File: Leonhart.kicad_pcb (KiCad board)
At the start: 8 copper layers, 34 parts, among them J1001 TC2050, J1002 Conn_01x03_Pin, J2001 TC2050, J2002 Conn_01x06_Pin, J2003 SMA-KWE901, J3002 TC2050, J3003 Conn_01x06_Pin, J3004 SMA-KWE901, J7001 USB_C_Receptacle_USB2.0_16P, J7002 USB_A, J7003 Micro_SD_Card_Det1, Q6001 DMG1012T, Q6002 DMG1012T, U1001 AM6231ASGGGAALW, U1002 SN74LVC2G241DCUR, U1003 AT24C32D-STUM-T, U2001 CC2652PSIP, U3001 nRF52840, U4001 TPS6521903RHBR, U4002 TLV62595DMQR, U5001 K4AAG165WA-BCWE, U6001 HR911130A, U6002 RTL8211F-CG, U7001 TVS0500DRVR, U7002 EMMC16G-TB29-PZ90, U7004 TPD3S014, U7005 TPS22918DBVR, X1001 32.768kHz, X1002 25MHz, X3001 32.768kHz, X3002 32MHz, X6001 ECS-2520MV-250-BN-TR

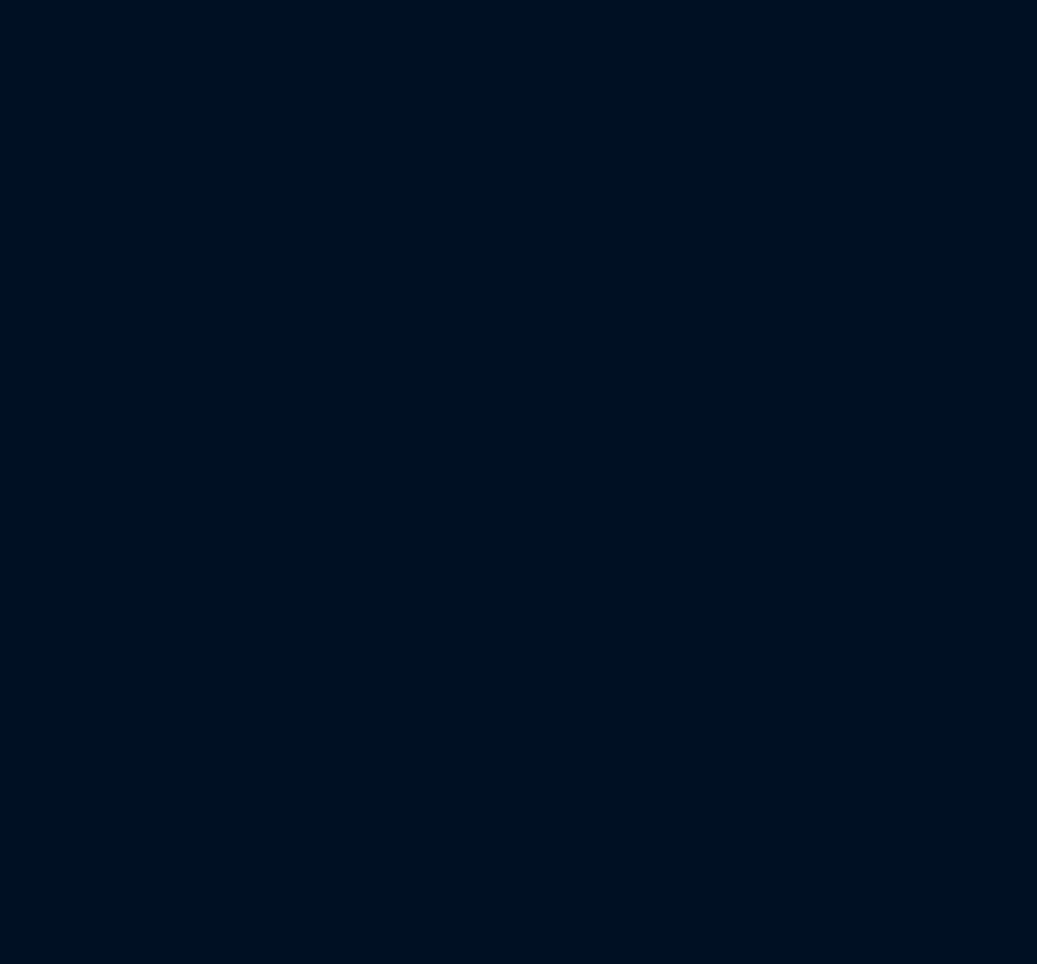
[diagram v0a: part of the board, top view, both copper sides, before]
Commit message: Added capcitor footprints
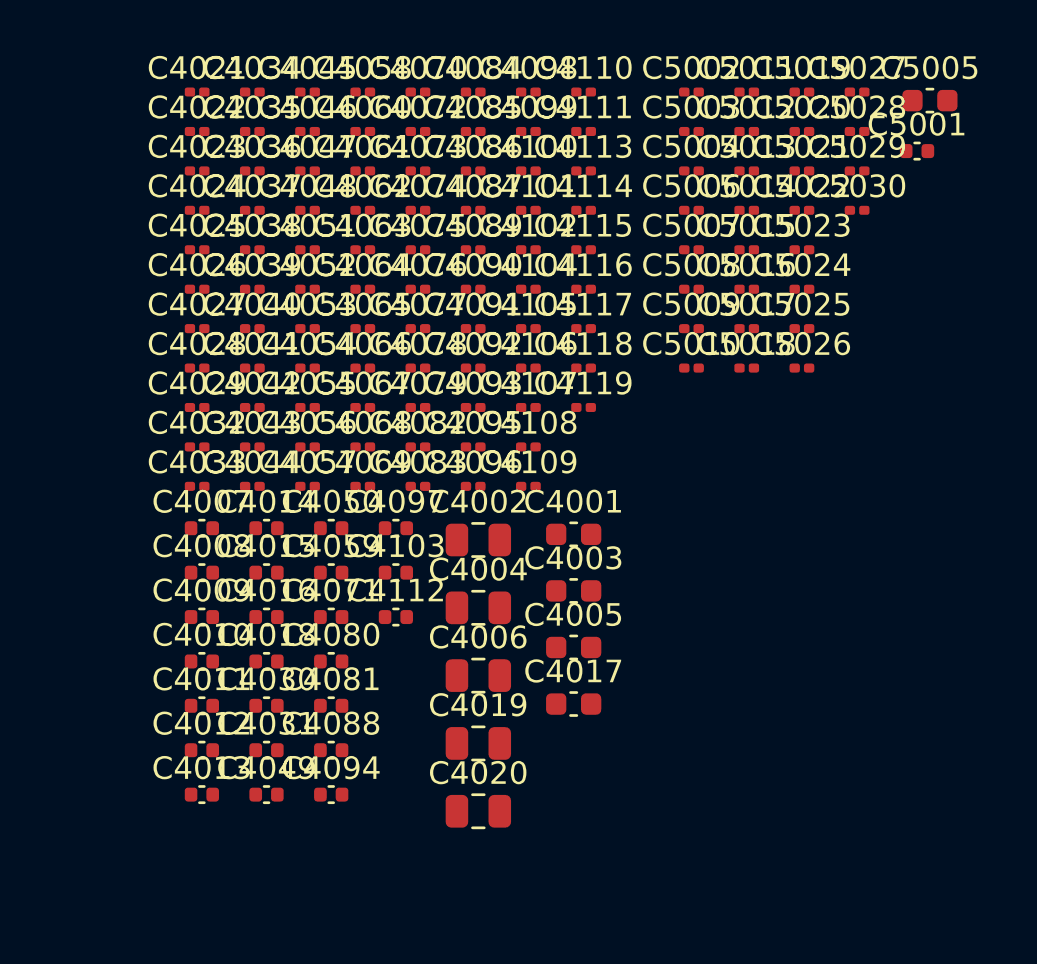
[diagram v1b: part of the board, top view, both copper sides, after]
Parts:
- added C4001: 10u, Capacitor_SMD:C_0603_1608Metric, F.Cu at (232.0, 70.1)
- added C4002: 47u, Capacitor_SMD:C_0805_2012Metric, F.Cu at (227.8, 70.4)
- added C4003: 10u, Capacitor_SMD:C_0603_1608Metric, F.Cu at (232.0, 72.6)
- added C4004: 47u, Capacitor_SMD:C_0805_2012Metric, F.Cu at (227.8, 73.4)
- added C4005: 10u, Capacitor_SMD:C_0603_1608Metric, F.Cu at (232.0, 75.1)
- added C4006: 47u, Capacitor_SMD:C_0805_2012Metric, F.Cu at (227.8, 76.4)
- added C4007: 2.2u, Capacitor_SMD:C_0402_1005Metric, F.Cu at (215.5, 69.8)
- added C4008: 2.2u, Capacitor_SMD:C_0402_1005Metric, F.Cu at (215.5, 71.8)
- added C4009: 2.2u, Capacitor_SMD:C_0402_1005Metric, F.Cu at (215.5, 73.8)
- added C4010: 2.2u, Capacitor_SMD:C_0402_1005Metric, F.Cu at (215.5, 75.8)
- added C4011: 2.2u, Capacitor_SMD:C_0402_1005Metric, F.Cu at (215.5, 77.7)
- added C4012: 2.2u, Capacitor_SMD:C_0402_1005Metric, F.Cu at (215.5, 79.7)
- added C4013: 2.2u, Capacitor_SMD:C_0402_1005Metric, F.Cu at (215.5, 81.7)
- added C4014: 2.2u, Capacitor_SMD:C_0402_1005Metric, F.Cu at (218.4, 69.8)
- added C4015: 2.2u, Capacitor_SMD:C_0402_1005Metric, F.Cu at (218.4, 71.8)
- added C4016: 2.2u, Capacitor_SMD:C_0402_1005Metric, F.Cu at (218.4, 73.8)
- added C4017: 10u, Capacitor_SMD:C_0603_1608Metric, F.Cu at (232.0, 77.7)
- added C4018: 120p, Capacitor_SMD:C_0402_1005Metric, F.Cu at (218.4, 75.8)
- added C4019: 22u, Capacitor_SMD:C_0805_2012Metric, F.Cu at (227.8, 79.4)
- added C4020: 22u, Capacitor_SMD:C_0805_2012Metric, F.Cu at (227.8, 82.4)
- added C4021: 1u, Capacitor_SMD:C_0201_0603Metric, F.Cu at (215.3, 50.5)
- added C4022: 1u, Capacitor_SMD:C_0201_0603Metric, F.Cu at (215.3, 52.2)
- added C4023: 1u, Capacitor_SMD:C_0201_0603Metric, F.Cu at (215.3, 54.0)
- added C4024: 1u, Capacitor_SMD:C_0201_0603Metric, F.Cu at (215.3, 55.7)
- added C4025: 1u, Capacitor_SMD:C_0201_0603Metric, F.Cu at (215.3, 57.5)
- added C4026: 1u, Capacitor_SMD:C_0201_0603Metric, F.Cu at (215.3, 59.2)
- added C4027: 1u, Capacitor_SMD:C_0201_0603Metric, F.Cu at (215.3, 61.0)
- added C4028: 1u, Capacitor_SMD:C_0201_0603Metric, F.Cu at (215.3, 62.7)
- added C4029: 1u, Capacitor_SMD:C_0201_0603Metric, F.Cu at (215.3, 64.5)
- added C4030: 10u, Capacitor_SMD:C_0402_1005Metric, F.Cu at (218.4, 77.7)
- added C4031: 4.7u, Capacitor_SMD:C_0402_1005Metric, F.Cu at (218.4, 79.7)
- added C4032: 1u, Capacitor_SMD:C_0201_0603Metric, F.Cu at (215.3, 66.2)
- added C4033: 0.1u, Capacitor_SMD:C_0201_0603Metric, F.Cu at (215.3, 68.0)
- added C4034: 0.1u, Capacitor_SMD:C_0201_0603Metric, F.Cu at (217.8, 50.5)
- added C4035: 0.1u, Capacitor_SMD:C_0201_0603Metric, F.Cu at (217.8, 52.2)
- added C4036: 0.1u, Capacitor_SMD:C_0201_0603Metric, F.Cu at (217.8, 54.0)
- added C4037: 0.1u, Capacitor_SMD:C_0201_0603Metric, F.Cu at (217.8, 55.7)
- added C4038: 0.1u, Capacitor_SMD:C_0201_0603Metric, F.Cu at (217.8, 57.5)
- added C4039: 0.1u, Capacitor_SMD:C_0201_0603Metric, F.Cu at (217.8, 59.2)
- added C4040: 0.1u, Capacitor_SMD:C_0201_0603Metric, F.Cu at (217.8, 61.0)
- added C4041: 0.1u, Capacitor_SMD:C_0201_0603Metric, F.Cu at (217.8, 62.7)
- added C4042: 0.1u, Capacitor_SMD:C_0201_0603Metric, F.Cu at (217.8, 64.5)
- added C4043: 0.1u, Capacitor_SMD:C_0201_0603Metric, F.Cu at (217.8, 66.2)
- added C4044: 0.1u, Capacitor_SMD:C_0201_0603Metric, F.Cu at (217.8, 68.0)
- added C4045: 0.1u, Capacitor_SMD:C_0201_0603Metric, F.Cu at (220.2, 50.5)
- added C4046: 0.1u, Capacitor_SMD:C_0201_0603Metric, F.Cu at (220.2, 52.2)
- added C4047: 0.1u, Capacitor_SMD:C_0201_0603Metric, F.Cu at (220.2, 54.0)
- added C4048: 0.1u, Capacitor_SMD:C_0201_0603Metric, F.Cu at (220.2, 55.7)
- added C4049: 10u, Capacitor_SMD:C_0402_1005Metric, F.Cu at (218.4, 81.7)
- added C4050: 4.7u, Capacitor_SMD:C_0402_1005Metric, F.Cu at (221.3, 69.8)
- added C4051: 0.1u, Capacitor_SMD:C_0201_0603Metric, F.Cu at (220.2, 57.5)
- added C4052: 0.1u, Capacitor_SMD:C_0201_0603Metric, F.Cu at (220.2, 59.2)
- added C4053: 0.1u, Capacitor_SMD:C_0201_0603Metric, F.Cu at (220.2, 61.0)
- added C4054: 0.1u, Capacitor_SMD:C_0201_0603Metric, F.Cu at (220.2, 62.7)
- added C4055: 0.1u, Capacitor_SMD:C_0201_0603Metric, F.Cu at (220.2, 64.5)
- added C4056: 0.1u, Capacitor_SMD:C_0201_0603Metric, F.Cu at (220.2, 66.2)
- added C4057: 0.1u, Capacitor_SMD:C_0201_0603Metric, F.Cu at (220.2, 68.0)
- added C4058: 0.1u, Capacitor_SMD:C_0201_0603Metric, F.Cu at (222.7, 50.5)
- added C4059: 4.7u, Capacitor_SMD:C_0402_1005Metric, F.Cu at (221.3, 71.8)
- added C4060: 1u, Capacitor_SMD:C_0201_0603Metric, F.Cu at (222.7, 52.2)
- added C4061: 0.1u, Capacitor_SMD:C_0201_0603Metric, F.Cu at (222.7, 54.0)
- added C4062: 0.1u, Capacitor_SMD:C_0201_0603Metric, F.Cu at (222.7, 55.7)
- added C4063: 0.1u, Capacitor_SMD:C_0201_0603Metric, F.Cu at (222.7, 57.5)
- added C4064: 0.1u, Capacitor_SMD:C_0201_0603Metric, F.Cu at (222.7, 59.2)
- added C4065: 0.1u, Capacitor_SMD:C_0201_0603Metric, F.Cu at (222.7, 61.0)
- added C4066: 0.1u, Capacitor_SMD:C_0201_0603Metric, F.Cu at (222.7, 62.7)
- added C4067: 0.1u, Capacitor_SMD:C_0201_0603Metric, F.Cu at (222.7, 64.5)
- added C4068: 0.1u, Capacitor_SMD:C_0201_0603Metric, F.Cu at (222.7, 66.2)
- added C4069: 0.1u, Capacitor_SMD:C_0201_0603Metric, F.Cu at (222.7, 68.0)
- added C4070: 0.1u, Capacitor_SMD:C_0201_0603Metric, F.Cu at (225.1, 50.5)
- added C4071: 4.7u, Capacitor_SMD:C_0402_1005Metric, F.Cu at (221.3, 73.8)
- added C4072: 1u, Capacitor_SMD:C_0201_0603Metric, F.Cu at (225.1, 52.2)
- added C4073: 0.1u, Capacitor_SMD:C_0201_0603Metric, F.Cu at (225.1, 54.0)
- added C4074: 0.1u, Capacitor_SMD:C_0201_0603Metric, F.Cu at (225.1, 55.7)
- added C4075: 0.1u, Capacitor_SMD:C_0201_0603Metric, F.Cu at (225.1, 57.5)
- added C4076: 0.1u, Capacitor_SMD:C_0201_0603Metric, F.Cu at (225.1, 59.2)
- added C4077: 0.1u, Capacitor_SMD:C_0201_0603Metric, F.Cu at (225.1, 61.0)
- added C4078: 0.1u, Capacitor_SMD:C_0201_0603Metric, F.Cu at (225.1, 62.7)
- added C4079: 0.1u, Capacitor_SMD:C_0201_0603Metric, F.Cu at (225.1, 64.5)
- added C4080: 10u, Capacitor_SMD:C_0402_1005Metric, F.Cu at (221.3, 75.8)
- added C4081: 4.7u, Capacitor_SMD:C_0402_1005Metric, F.Cu at (221.3, 77.7)
- added C4082: 1u, Capacitor_SMD:C_0201_0603Metric, F.Cu at (225.1, 66.2)
- added C4083: 0.1u, Capacitor_SMD:C_0201_0603Metric, F.Cu at (225.1, 68.0)
- added C4084: 0.1u, Capacitor_SMD:C_0201_0603Metric, F.Cu at (227.6, 50.5)
- added C4085: 0.1u, Capacitor_SMD:C_0201_0603Metric, F.Cu at (227.6, 52.2)
- added C4086: 0.1u, Capacitor_SMD:C_0201_0603Metric, F.Cu at (227.6, 54.0)
- added C4087: 0.1u, Capacitor_SMD:C_0201_0603Metric, F.Cu at (227.6, 55.7)
- added C4088: 4.7u, Capacitor_SMD:C_0402_1005Metric, F.Cu at (221.3, 79.7)
- added C4089: 0.1u, Capacitor_SMD:C_0201_0603Metric, F.Cu at (227.6, 57.5)
- added C4090: 0.01u, Capacitor_SMD:C_0201_0603Metric, F.Cu at (227.6, 59.2)
- added C4091: 1u, Capacitor_SMD:C_0201_0603Metric, F.Cu at (227.6, 61.0)
- added C4092: 0.1u, Capacitor_SMD:C_0201_0603Metric, F.Cu at (227.6, 62.7)
- added C4093: 0.01u, Capacitor_SMD:C_0201_0603Metric, F.Cu at (227.6, 64.5)
- added C4094: 4.7u, Capacitor_SMD:C_0402_1005Metric, F.Cu at (221.3, 81.7)
- added C4095: 0.1u, Capacitor_SMD:C_0201_0603Metric, F.Cu at (227.6, 66.2)
- added C4096: 0.01u, Capacitor_SMD:C_0201_0603Metric, F.Cu at (227.6, 68.0)
- added C4097: 4.7u, Capacitor_SMD:C_0402_1005Metric, F.Cu at (224.1, 69.8)
- added C4098: 0.1u, Capacitor_SMD:C_0201_0603Metric, F.Cu at (230.0, 50.5)
- added C4099: 0.01u, Capacitor_SMD:C_0201_0603Metric, F.Cu at (230.0, 52.2)
- added C4100: 1u, Capacitor_SMD:C_0201_0603Metric, F.Cu at (230.0, 54.0)
- added C4101: 0.1u, Capacitor_SMD:C_0201_0603Metric, F.Cu at (230.0, 55.7)
- added C4102: 0.01u, Capacitor_SMD:C_0201_0603Metric, F.Cu at (230.0, 57.5)
- added C4103: 4.7u, Capacitor_SMD:C_0402_1005Metric, F.Cu at (224.1, 71.8)
- added C4104: 0.1u, Capacitor_SMD:C_0201_0603Metric, F.Cu at (230.0, 59.2)
- added C4105: 0.01u, Capacitor_SMD:C_0201_0603Metric, F.Cu at (230.0, 61.0)
- added C4106: 1u, Capacitor_SMD:C_0201_0603Metric, F.Cu at (230.0, 62.7)
- added C4107: 0.1u, Capacitor_SMD:C_0201_0603Metric, F.Cu at (230.0, 64.5)
- added C4108: 0.01u, Capacitor_SMD:C_0201_0603Metric, F.Cu at (230.0, 66.2)
- added C4109: 1u, Capacitor_SMD:C_0201_0603Metric, F.Cu at (230.0, 68.0)
- added C4110: 0.1u, Capacitor_SMD:C_0201_0603Metric, F.Cu at (232.5, 50.5)
- added C4111: 0.01u, Capacitor_SMD:C_0201_0603Metric, F.Cu at (232.5, 52.2)
- added C4112: 4.7u, Capacitor_SMD:C_0402_1005Metric, F.Cu at (224.1, 73.8)
- added C4113: 0.1u, Capacitor_SMD:C_0201_0603Metric, F.Cu at (232.5, 54.0)
- added C4114: 0.01u, Capacitor_SMD:C_0201_0603Metric, F.Cu at (232.5, 55.7)
- added C4115: 1u, Capacitor_SMD:C_0201_0603Metric, F.Cu at (232.5, 57.5)
- added C4116: 0.1u, Capacitor_SMD:C_0201_0603Metric, F.Cu at (232.5, 59.2)
- added C4117: 0.01u, Capacitor_SMD:C_0201_0603Metric, F.Cu at (232.5, 61.0)
- added C4118: 0.1u, Capacitor_SMD:C_0201_0603Metric, F.Cu at (232.5, 62.7)
- added C4119: 0.1u, Capacitor_SMD:C_0201_0603Metric, F.Cu at (232.5, 64.5)
- added C5001: 2.2u, Capacitor_SMD:C_0402_1005Metric, F.Cu at (247.3, 53.1)
- added C5002: 0.1u, Capacitor_SMD:C_0201_0603Metric, F.Cu at (237.3, 50.5)
- added C5003: 0.1u, Capacitor_SMD:C_0201_0603Metric, F.Cu at (237.3, 52.2)
- added C5004: 0.01u, Capacitor_SMD:C_0201_0603Metric, F.Cu at (237.3, 54.0)
- added C5005: 22u, Capacitor_SMD:C_0603_1608Metric, F.Cu at (247.8, 50.9)
- added C5006: 0.1u, Capacitor_SMD:C_0201_0603Metric, F.Cu at (237.3, 55.7)
- added C5007: 0.1u, Capacitor_SMD:C_0201_0603Metric, F.Cu at (237.3, 57.5)
- added C5008: 0.1u, Capacitor_SMD:C_0201_0603Metric, F.Cu at (237.3, 59.2)
- added C5009: 0.1u, Capacitor_SMD:C_0201_0603Metric, F.Cu at (237.3, 61.0)
- added C5010: 0.1u, Capacitor_SMD:C_0201_0603Metric, F.Cu at (237.3, 62.7)
- added C5011: 0.1u, Capacitor_SMD:C_0201_0603Metric, F.Cu at (239.7, 50.5)
- added C5012: 0.1u, Capacitor_SMD:C_0201_0603Metric, F.Cu at (239.7, 52.2)
- added C5013: 0.1u, Capacitor_SMD:C_0201_0603Metric, F.Cu at (239.7, 54.0)
- added C5014: 0.1u, Capacitor_SMD:C_0201_0603Metric, F.Cu at (239.7, 55.7)
- added C5015: 0.1u, Capacitor_SMD:C_0201_0603Metric, F.Cu at (239.7, 57.5)
- added C5016: 0.1u, Capacitor_SMD:C_0201_0603Metric, F.Cu at (239.7, 59.2)
- added C5017: 0.1u, Capacitor_SMD:C_0201_0603Metric, F.Cu at (239.7, 61.0)
- added C5018: 0.1u, Capacitor_SMD:C_0201_0603Metric, F.Cu at (239.7, 62.7)
- added C5019: 0.1u, Capacitor_SMD:C_0201_0603Metric, F.Cu at (242.2, 50.5)
- added C5020: 0.1u, Capacitor_SMD:C_0201_0603Metric, F.Cu at (242.2, 52.2)
- added C5021: 0.1u, Capacitor_SMD:C_0201_0603Metric, F.Cu at (242.2, 54.0)
- added C5022: 1n, Capacitor_SMD:C_0201_0603Metric, F.Cu at (242.2, 55.7)
- added C5023: 1n, Capacitor_SMD:C_0201_0603Metric, F.Cu at (242.2, 57.5)
- added C5024: 100p, Capacitor_SMD:C_0201_0603Metric, F.Cu at (242.2, 59.2)
- added C5025: 100p, Capacitor_SMD:C_0201_0603Metric, F.Cu at (242.2, 61.0)
- added C5026: 47p, Capacitor_SMD:C_0201_0603Metric, F.Cu at (242.2, 62.7)
- added C5027: 47p, Capacitor_SMD:C_0201_0603Metric, F.Cu at (244.6, 50.5)
- added C5028: 10p, Capacitor_SMD:C_0201_0603Metric, F.Cu at (244.6, 52.2)
- added C5029: 10p, Capacitor_SMD:C_0201_0603Metric, F.Cu at (244.6, 54.0)
- added C5030: 10p, Capacitor_SMD:C_0201_0603Metric, F.Cu at (244.6, 55.7)

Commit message: Added almost all passive component footprints
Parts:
- added C1001: 0.1u, Capacitor_SMD:C_0201_0603Metric, F.Cu at (269.6, 70.0)
- added C1002: 20p, Capacitor_SMD:C_0402_1005Metric, F.Cu at (266.9, 70.1)
- added C1003: 20p, Capacitor_SMD:C_0402_1005Metric, F.Cu at (266.9, 72.1)
- added C1004: 18p, Capacitor_SMD:C_0402_1005Metric, F.Cu at (266.9, 74.1)
- added C1005: 0.1u, Capacitor_SMD:C_0201_0603Metric, F.Cu at (269.6, 71.8)
- added C1006: 18p, Capacitor_SMD:C_0402_1005Metric, F.Cu at (266.9, 76.0)
- added C1007: 0.1u, Capacitor_SMD:C_0201_0603Metric, F.Cu at (269.6, 73.5)
- added C1008: C, Capacitor_SMD:C_0402_1005Metric, F.Cu at (129.7, 165.6)
- added C1009: C, Capacitor_SMD:C_0402_1005Metric, F.Cu at (129.7, 167.6)
- added C2001: 0.1u, Capacitor_SMD:C_0201_0603Metric, F.Cu at (266.7, 79.9)
- added C2002: 15p, Capacitor_SMD:C_0201_0603Metric, F.Cu at (266.7, 81.7)
- added C3001: 4.7u, Capacitor_SMD:C_0402_1005Metric, F.Cu at (121.4, 169.2)
- added C3002: 0.1u, Capacitor_SMD:C_0201_0603Metric, F.Cu at (125.1, 165.5)
- added C3003: 100p, Capacitor_SMD:C_0201_0603Metric, F.Cu at (125.1, 167.2)
- added C3004: 0.1u, Capacitor_SMD:C_0201_0603Metric, F.Cu at (185.7, 51.0)
- added C3005: 1u, Capacitor_SMD:C_0603_1608Metric, F.Cu at (182.4, 51.3)
- added C3006: 47n, Capacitor_SMD:C_0201_0603Metric, F.Cu at (185.7, 52.7)
- added C3007: 4.7u, Capacitor_SMD:C_0603_1608Metric, F.Cu at (182.4, 53.8)
- added C3008: 0.8p, Capacitor_SMD:C_0201_0603Metric, F.Cu at (185.7, 54.5)
- added C3009: 0.5p, Capacitor_SMD:C_0201_0603Metric, F.Cu at (185.7, 56.2)
- added C3011: 8p, Capacitor_SMD:C_0201_0603Metric, F.Cu at (185.7, 58.0)
- added C3012: 8p, Capacitor_SMD:C_0201_0603Metric, F.Cu at (188.1, 51.0)
- added C3013: 12p, Capacitor_SMD:C_0201_0603Metric, F.Cu at (188.1, 52.7)
- added C3014: 12p, Capacitor_SMD:C_0201_0603Metric, F.Cu at (188.1, 54.5)
- added C3015: 0.1u, Capacitor_SMD:C_0201_0603Metric, F.Cu at (188.1, 56.2)
- added C3016: 1u, Capacitor_SMD:C_0603_1608Metric, F.Cu at (182.4, 56.4)
- added C3017: 0.1u, Capacitor_SMD:C_0201_0603Metric, F.Cu at (188.1, 58.0)
- added C3018: 0.1u, Capacitor_SMD:C_0201_0603Metric, F.Cu at (190.6, 51.0)
- added C3019: 0.1u, Capacitor_SMD:C_0201_0603Metric, F.Cu at (190.6, 52.7)
- added C7001: 4.7u, Capacitor_SMD:C_0402_1005Metric, F.Cu at (258.1, 76.2)
- added C7002: 0.1u, Capacitor_SMD:C_0201_0603Metric, F.Cu at (250.5, 70.0)
- added C7003: 0.1u, Capacitor_SMD:C_0201_0603Metric, F.Cu at (250.5, 71.8)
- added C7004: 0.1u, Capacitor_SMD:C_0201_0603Metric, F.Cu at (250.5, 73.5)
- added C7005: 0.1u, Capacitor_SMD:C_0201_0603Metric, F.Cu at (250.5, 75.3)
- added C7006: 0.1u, Capacitor_SMD:C_0201_0603Metric, F.Cu at (250.5, 77.0)
- added C7007: 0.1u, Capacitor_SMD:C_0201_0603Metric, F.Cu at (252.9, 70.0)
- added C7008: 0.1u, Capacitor_SMD:C_0201_0603Metric, F.Cu at (252.9, 71.8)
- added C7009: 0.1u, Capacitor_SMD:C_0201_0603Metric, F.Cu at (252.9, 73.5)
- added C7010: 0.1u, Capacitor_SMD:C_0201_0603Metric, F.Cu at (252.9, 75.3)
- added C7011: 4.7u, Capacitor_SMD:C_0402_1005Metric, F.Cu at (258.1, 78.1)
- added C7012: 10u, Capacitor_SMD:C_0603_1608Metric, F.Cu at (261.5, 76.4)
- added C7013: 0.1u, Capacitor_SMD:C_0201_0603Metric, F.Cu at (252.9, 77.0)
- added C7014: 0.1u, Capacitor_SMD:C_0201_0603Metric, F.Cu at (255.4, 70.0)
- added C7015: 10u, Capacitor_SMD:C_0603_1608Metric, F.Cu at (261.5, 78.9)
- added C7016: 0.1u, Capacitor_SMD:C_0201_0603Metric, F.Cu at (255.4, 71.8)
- added C7017: 100u, Capacitor_SMD:C_1206_3216Metric, F.Cu at (252.1, 79.6)
- added C7018: 4.7u, Capacitor_SMD:C_0402_1005Metric, F.Cu at (258.1, 80.1)
- added C7019: 0.1u, Capacitor_SMD:C_0201_0603Metric, F.Cu at (255.4, 73.5)
- added C7020: 0.1u, Capacitor_SMD:C_0201_0603Metric, F.Cu at (255.4, 75.3)
- added C7021: 22u, Capacitor_SMD:C_0805_2012Metric, F.Cu at (258.9, 70.7)
- added C7022: 22u, Capacitor_SMD:C_0805_2012Metric, F.Cu at (258.9, 73.7)
- added D1001: D, Diode_SMD:D_SOD-523, F.Cu at (150.2, 45.6)
- added D1002: D_TVS, Diode_SMD:D_SOD-882, F.Cu at (126.7, 46.6)
- added D1003: D_TVS, Diode_SMD:D_SOD-882, F.Cu at (126.7, 49.0)
- added D1004: D, Diode_SMD:D_SOD-523, F.Cu at (150.2, 48.1)
- added D1005: D, Diode_SMD:D_SOD-523, F.Cu at (150.2, 50.5)
- added D1006: D, Diode_SMD:D_SOD-523, F.Cu at (150.2, 53.0)
- added D2001: D, Diode_SMD:D_SOD-523, F.Cu at (155.8, 45.6)
- added D2002: D, Diode_SMD:D_SOD-523, F.Cu at (155.8, 48.1)
- added D2003: D, Diode_SMD:D_SOD-523, F.Cu at (155.8, 50.5)
- added D6001: D, Diode_SMD:D_SOD-523, F.Cu at (155.8, 55.0)
- added D6002: D, Diode_SMD:D_SOD-523, F.Cu at (155.8, 57.5)
- added D6003: D, Diode_SMD:D_SOD-523, F.Cu at (155.8, 59.9)
- added D7001: D_TVS, Diode_SMD:D_SOD-882, F.Cu at (116.6, 46.6)
- added D7002: D_TVS, Diode_SMD:D_SOD-882, F.Cu at (116.6, 49.0)
- added D7003: D, Diode_SMD:D_SOD-523, F.Cu at (144.6, 45.6)
- added D7004: D, Diode_SMD:D_SOD-523, F.Cu at (144.6, 48.1)
- added D7005: D, Diode_SMD:D_SOD-523, F.Cu at (144.6, 50.5)
- added D7006: D_TVS, Diode_SMD:D_SOD-882, F.Cu at (116.6, 51.3)
- added D7007: D_TVS, Diode_SMD:D_SOD-882, F.Cu at (119.3, 46.6)
- added D7008: D_TVS, Diode_SMD:D_SOD-882, F.Cu at (119.3, 49.0)
- added D7009: D_TVS, Diode_SMD:D_SOD-882, F.Cu at (119.3, 51.3)
- added D7010: D_TVS, Diode_SMD:D_SOD-882, F.Cu at (122.0, 46.6)
- added D7011: D_TVS, Diode_SMD:D_SOD-882, F.Cu at (122.0, 49.0)
- added D7012: D_TVS, Diode_SMD:D_SOD-882, F.Cu at (122.0, 51.3)
- added D7013: D, Diode_SMD:D_SOD-523, F.Cu at (144.6, 53.0)
- added D7014: D, Diode_SMD:D_SOD-523, F.Cu at (144.6, 55.5)
- added FB2001: 120R, Resistor_SMD:R_0402_1005Metric, F.Cu at (259.4, 100.4)
- added FB3001: 120R, Resistor_SMD:R_0402_1005Metric, F.Cu at (229.7, 129.8)
- added FB4001: 120R, Resistor_SMD:R_0402_1005Metric, F.Cu at (245.8, 100.4)
- added FB4002: 120R, Resistor_SMD:R_0402_1005Metric, F.Cu at (245.8, 102.4)
- added FB4003: 120R, Resistor_SMD:R_0402_1005Metric, F.Cu at (245.8, 104.4)
- added FB4004: 120R, Resistor_SMD:R_0402_1005Metric, F.Cu at (245.8, 106.4)
- added FB4005: 120R, Resistor_SMD:R_0402_1005Metric, F.Cu at (245.8, 108.3)
- added FB4006: 120R, Resistor_SMD:R_0402_1005Metric, F.Cu at (245.8, 110.3)
- added FB4007: 120R, Resistor_SMD:R_0402_1005Metric, F.Cu at (245.8, 112.3)
- added FB4008: 120R, Resistor_SMD:R_0402_1005Metric, F.Cu at (248.7, 100.4)
- added FB4009: 120R, Resistor_SMD:R_0402_1005Metric, F.Cu at (248.7, 102.4)
- added FB4010: 120R, Resistor_SMD:R_0402_1005Metric, F.Cu at (248.7, 104.4)
- added FB4011: 120R, Resistor_SMD:R_0402_1005Metric, F.Cu at (248.7, 106.4)
- added FB5001: 120R, Resistor_SMD:R_0402_1005Metric, F.Cu at (229.7, 118.3)
- added FB6001: 120R, Resistor_SMD:R_0402_1005Metric, F.Cu at (240.4, 118.3)
- added FB6002: 120R, Resistor_SMD:R_0402_1005Metric, F.Cu at (240.4, 120.3)
- added FB6003: 120R, Resistor_SMD:R_0402_1005Metric, F.Cu at (240.4, 122.3)
- added L3001: 10u, Inductor_SMD:L_0603_1608Metric, F.Cu at (182.4, 58.9)
- added L3002: 15n, Inductor_SMD:L_0402_1005Metric, F.Cu at (185.9, 59.8)
- added L3003: 10u, Inductor_SMD:L_0603_1608Metric, F.Cu at (182.4, 61.4)
- added L3004: 4.7n, Inductor_SMD:L_0201_0603Metric, F.Cu at (190.6, 54.5)
- added L4001: 0.33u, Inductor_SMD:L_1008_2520Metric, F.Cu at (100.1, 46.1)
- added L4002: 0.47u, Inductor_SMD:L_1008_2520Metric, F.Cu at (100.1, 49.9)
- added L4003: 0.47u, Inductor_SMD:L_1008_2520Metric, F.Cu at (100.1, 53.6)
- added L4004: 0.47u, Inductor_SMD:L_1008_2520Metric, F.Cu at (100.1, 57.4)
- added R1001: 10k, Resistor_SMD:R_0402_1005Metric, F.Cu at (245.8, 116.3)
- added R1002: 10k, Resistor_SMD:R_0402_1005Metric, F.Cu at (245.8, 118.3)
- added R1003: 10k, Resistor_SMD:R_0402_1005Metric, F.Cu at (245.8, 120.3)
- added R1004: 10k, Resistor_SMD:R_0402_1005Metric, F.Cu at (245.8, 122.3)
- added R1005: 10k, Resistor_SMD:R_0402_1005Metric, F.Cu at (245.8, 124.3)
- added R1006: 10k, Resistor_SMD:R_0402_1005Metric, F.Cu at (245.8, 126.3)
- added R1007: 10k, Resistor_SMD:R_0402_1005Metric, F.Cu at (245.8, 128.3)
- added R1008: 10k, Resistor_SMD:R_0402_1005Metric, F.Cu at (248.7, 116.3)
- added R1009: 2.2k, Resistor_SMD:R_0402_1005Metric, F.Cu at (248.7, 118.3)
- added R1010: 2.2k, Resistor_SMD:R_0402_1005Metric, F.Cu at (248.7, 120.3)
- added R1011: 33R, Resistor_SMD:R_0201_0603Metric, F.Cu at (254.3, 116.2)
- added R1012: 0R, Resistor_SMD:R_0402_1005Metric, F.Cu at (248.7, 122.3)
- added R1013: 10k, Resistor_SMD:R_0402_1005Metric, F.Cu at (248.7, 124.3)
- added R1014: 10k, Resistor_SMD:R_0402_1005Metric, F.Cu at (248.7, 126.3)
- added R1015: R, Resistor_SMD:R_0402_1005Metric, F.Cu at (248.7, 128.3)
- added R1016: R, Resistor_SMD:R_0201_0603Metric, F.Cu at (254.3, 118.0)
- added R1017: R, Resistor_SMD:R_0201_0603Metric, F.Cu at (254.3, 119.7)
- added R1018: 10k, Resistor_SMD:R_0201_0603Metric, F.Cu at (254.3, 121.5)
- added R1019: R, Resistor_SMD:R_0201_0603Metric, F.Cu at (254.3, 123.2)
- added R1020: 10k, Resistor_SMD:R_0201_0603Metric, F.Cu at (254.3, 125.0)
- added R1021: 10k, Resistor_SMD:R_0201_0603Metric, F.Cu at (254.3, 126.7)
- added R1022: R, Resistor_SMD:R_0201_0603Metric, F.Cu at (256.8, 116.2)
- added R1023: 10k, Resistor_SMD:R_0201_0603Metric, F.Cu at (256.8, 118.0)
- added R1024: R, Resistor_SMD:R_0201_0603Metric, F.Cu at (256.8, 119.7)
- added R1025: 10k, Resistor_SMD:R_0201_0603Metric, F.Cu at (256.8, 121.5)
- added R1026: R, Resistor_SMD:R_0201_0603Metric, F.Cu at (256.8, 123.2)
- added R1027: R, Resistor_SMD:R_0201_0603Metric, F.Cu at (256.8, 125.0)
- added R1028: 10k, Resistor_SMD:R_0201_0603Metric, F.Cu at (256.8, 126.7)
- added R1029: R, Resistor_SMD:R_0201_0603Metric, F.Cu at (259.2, 116.2)
- added R1030: 10k, Resistor_SMD:R_0201_0603Metric, F.Cu at (259.2, 118.0)
- added R1031: 10k, Resistor_SMD:R_0201_0603Metric, F.Cu at (259.2, 119.7)
- added R1032: 10k, Resistor_SMD:R_0201_0603Metric, F.Cu at (259.2, 121.5)
- added R1033: 10k, Resistor_SMD:R_0201_0603Metric, F.Cu at (259.2, 123.2)
- added R1034: R, Resistor_SMD:R_0201_0603Metric, F.Cu at (259.2, 125.0)
- added R1035: 10k, Resistor_SMD:R_0201_0603Metric, F.Cu at (259.2, 126.7)
- added R1036: R, Resistor_SMD:R_0201_0603Metric, F.Cu at (261.7, 116.2)
- added R1037: R, Resistor_SMD:R_0201_0603Metric, F.Cu at (261.7, 118.0)
- added R1038: R, Resistor_SMD:R_0201_0603Metric, F.Cu at (261.7, 119.7)
- added R1039: 10k, Resistor_SMD:R_0201_0603Metric, F.Cu at (261.7, 121.5)
- added R1040: 10k, Resistor_SMD:R_0201_0603Metric, F.Cu at (261.7, 123.2)
- added R1041: R, Resistor_SMD:R_0201_0603Metric, F.Cu at (261.7, 125.0)
- added R1042: 10k, Resistor_SMD:R_0201_0603Metric, F.Cu at (261.7, 126.7)
- added R1043: 10k, Resistor_SMD:R_0201_0603Metric, F.Cu at (264.1, 116.2)
- added R1044: R, Resistor_SMD:R_0201_0603Metric, F.Cu at (264.1, 118.0)
- added R1045: 10k, Resistor_SMD:R_0201_0603Metric, F.Cu at (264.1, 119.7)
- added R1046: R, Resistor_SMD:R_0201_0603Metric, F.Cu at (264.1, 121.5)
- added R1047: R, Resistor_SMD:R_0201_0603Metric, F.Cu at (264.1, 123.2)
- added R1048: 10k, Resistor_SMD:R_0402_1005Metric, F.Cu at (251.6, 116.3)
- added R1049: 1k, Resistor_SMD:R_0402_1005Metric, F.Cu at (251.6, 118.3)
- added R1050: 1k, Resistor_SMD:R_0402_1005Metric, F.Cu at (251.6, 120.3)
- added R1051: 1k, Resistor_SMD:R_0402_1005Metric, F.Cu at (251.6, 122.3)
- added R2001: 0R, Resistor_SMD:R_0402_1005Metric, F.Cu at (259.4, 102.4)
- added R2002: 0R, Resistor_SMD:R_0402_1005Metric, F.Cu at (259.4, 104.4)
- added R2003: 0R, Resistor_SMD:R_0402_1005Metric, F.Cu at (259.4, 106.4)
- added R2004: 0R, Resistor_SMD:R_0402_1005Metric, F.Cu at (259.4, 108.3)
- added R3001: 10k, Resistor_SMD:R_0201_0603Metric, F.Cu at (190.6, 56.2)
- added R4001: 0R, Resistor_SMD:R_0402_1005Metric, F.Cu at (248.7, 108.3)
- added R4002: 100k, Resistor_SMD:R_0402_1005Metric, F.Cu at (248.7, 110.3)
- added R4003: 11k, Resistor_SMD:R_0402_1005Metric, F.Cu at (248.7, 112.3)
- added R4004: 10k, Resistor_SMD:R_0402_1005Metric, F.Cu at (251.6, 100.4)
- added R4005: 10k, Resistor_SMD:R_0402_1005Metric, F.Cu at (251.6, 102.4)
- added R4006: 10k, Resistor_SMD:R_0402_1005Metric, F.Cu at (251.6, 104.4)
- added R4007: 10k, Resistor_SMD:R_0402_1005Metric, F.Cu at (251.6, 106.4)
- added R4008: 10k, Resistor_SMD:R_0402_1005Metric, F.Cu at (251.6, 108.3)
- added R4009: 10k, Resistor_SMD:R_0402_1005Metric, F.Cu at (251.6, 110.3)
- added R4010: 10k, Resistor_SMD:R_0402_1005Metric, F.Cu at (251.6, 112.3)
- added R4011: 270k, Resistor_SMD:R_0402_1005Metric, F.Cu at (254.5, 100.4)
- added R4012: 180k, Resistor_SMD:R_0402_1005Metric, F.Cu at (254.5, 102.4)
- added R4013: 100k, Resistor_SMD:R_0402_1005Metric, F.Cu at (254.5, 104.4)
- added R4014: R, Resistor_SMD:R_0402_1005Metric, F.Cu at (254.5, 106.4)
- added R4015: 10k, Resistor_SMD:R_0402_1005Metric, F.Cu at (254.5, 108.3)
- added R5001: 33R, Resistor_SMD:R_0201_0603Metric, F.Cu at (229.5, 124.2)
- added R5002: 33R, Resistor_SMD:R_0201_0603Metric, F.Cu at (229.5, 125.9)
- added R5003: R, Resistor_SMD:R_0402_1005Metric, F.Cu at (229.7, 120.3)
- added R5004: 2.2k, Resistor_SMD:R_0402_1005Metric, F.Cu at (229.7, 122.3)
- added R5005: 10k, Resistor_SMD:R_0402_1005Metric, F.Cu at (232.6, 118.3)
- added R5006: 240R, Resistor_SMD:R_0402_1005Metric, F.Cu at (232.6, 120.3)
- added R5007: 240R, Resistor_SMD:R_0402_1005Metric, F.Cu at (232.6, 122.3)
- added R5008: 1k, Resistor_SMD:R_0402_1005Metric, F.Cu at (235.5, 118.3)
- added R5009: 1k, Resistor_SMD:R_0402_1005Metric, F.Cu at (235.5, 120.3)
- added R5010: 1k, Resistor_SMD:R_0402_1005Metric, F.Cu at (235.5, 122.3)
- added R7001: 22R, Resistor_SMD:R_0201_0603Metric, F.Cu at (241.1, 100.3)
- added R7002: 10k, Resistor_SMD:R_0402_1005Metric, F.Cu at (229.7, 100.4)
- added R7003: 20k, Resistor_SMD:R_0402_1005Metric, F.Cu at (229.7, 102.4)
- added R7004: 49.9k, Resistor_SMD:R_0402_1005Metric, F.Cu at (229.7, 104.4)
- added R7005: 49.9k, Resistor_SMD:R_0402_1005Metric, F.Cu at (229.7, 106.4)
- added R7006: 49.9k, Resistor_SMD:R_0402_1005Metric, F.Cu at (229.7, 108.3)
- added R7007: 49.9k, Resistor_SMD:R_0402_1005Metric, F.Cu at (229.7, 110.3)
- added R7008: 49.9k, Resistor_SMD:R_0402_1005Metric, F.Cu at (229.7, 112.3)
- added R7009: 49.9k, Resistor_SMD:R_0402_1005Metric, F.Cu at (229.7, 114.3)
- added R7010: 49.9k, Resistor_SMD:R_0402_1005Metric, F.Cu at (232.6, 100.4)
- added R7011: 49.9k, Resistor_SMD:R_0402_1005Metric, F.Cu at (232.6, 102.4)
- added R7012: 49.9k, Resistor_SMD:R_0402_1005Metric, F.Cu at (232.6, 104.4)
- added R7013: 49.9k, Resistor_SMD:R_0402_1005Metric, F.Cu at (232.6, 106.4)
- added R7014: 22R, Resistor_SMD:R_0201_0603Metric, F.Cu at (241.1, 102.0)
- added R7015: 499R, Resistor_SMD:R_0402_1005Metric, F.Cu at (232.6, 108.3)
- added R7016: 5.1k, Resistor_SMD:R_0402_1005Metric, F.Cu at (232.6, 110.3)
- added R7017: 5.1k, Resistor_SMD:R_0402_1005Metric, F.Cu at (232.6, 112.3)
- added R7018: 499R, Resistor_SMD:R_0402_1005Metric, F.Cu at (232.6, 114.3)
- added R7019: 49.9k, Resistor_SMD:R_0402_1005Metric, F.Cu at (235.5, 100.4)
- added R7020: 10k, Resistor_SMD:R_0402_1005Metric, F.Cu at (235.5, 102.4)
- added R7021: 20k, Resistor_SMD:R_0402_1005Metric, F.Cu at (235.5, 104.4)
- added R7022: 10k, Resistor_SMD:R_0402_1005Metric, F.Cu at (235.5, 106.4)
- added R7023: 1k, Resistor_SMD:R_0402_1005Metric, F.Cu at (235.5, 108.3)
- added R7024: 10k, Resistor_SMD:R_0402_1005Metric, F.Cu at (235.5, 110.3)
- added R7025: 10k, Resistor_SMD:R_0402_1005Metric, F.Cu at (235.5, 112.3)
- added R7026: 10k, Resistor_SMD:R_0402_1005Metric, F.Cu at (235.5, 114.3)
- added R7027: 10k, Resistor_SMD:R_0402_1005Metric, F.Cu at (238.4, 100.4)
- added R7028: 10k, Resistor_SMD:R_0402_1005Metric, F.Cu at (238.4, 102.4)
- added R7029: 10k, Resistor_SMD:R_0402_1005Metric, F.Cu at (238.4, 104.4)
- added R7030: 10k, Resistor_SMD:R_0402_1005Metric, F.Cu at (238.4, 106.4)
- added R7031: 10k, Resistor_SMD:R_0402_1005Metric, F.Cu at (238.4, 108.3)
- added R8001: 2.2k, Resistor_SMD:R_0402_1005Metric, F.Cu at (240.4, 126.3)
- added R8002: 2.2k, Resistor_SMD:R_0402_1005Metric, F.Cu at (240.4, 128.3)
- added TP1001: TestPoint, TestPoint:TestPoint_Pad_1.0x1.0mm, F.Cu at (243.2, 148.7)
- added TP1002: TestPoint, TestPoint:TestPoint_Pad_1.0x1.0mm, F.Cu at (243.2, 151.7)
- added TP4001: TestPoint, TestPoint:TestPoint_Pad_1.0x1.0mm, F.Cu at (243.2, 140.6)
- added TP4002: TestPoint, TestPoint:TestPoint_Pad_1.0x1.0mm, F.Cu at (243.2, 143.6)
- added TP4003: TestPoint, TestPoint:TestPoint_Pad_1.0x1.0mm, F.Cu at (246.3, 140.6)
- added TP4004: TestPoint, TestPoint:TestPoint_Pad_1.0x1.0mm, F.Cu at (246.3, 143.6)
- added TP4005: TestPoint, TestPoint:TestPoint_Pad_1.0x1.0mm, F.Cu at (249.3, 140.6)
- added TP4006: TestPoint, TestPoint:TestPoint_Pad_1.0x1.0mm, F.Cu at (249.3, 143.6)
- added TP4007: TestPoint, TestPoint:TestPoint_Pad_1.0x1.0mm, F.Cu at (252.4, 140.6)
- added TP4008: TestPoint, TestPoint:TestPoint_Pad_1.0x1.0mm, F.Cu at (252.4, 143.6)
- added TP6001: TestPoint, TestPoint:TestPoint_Pad_1.0x1.0mm, F.Cu at (248.3, 148.7)
- X3002: value 32MHz -> 25MHz
- moved U1001 13.0 mm to (139.0, 73.8)
- moved X3002 9.29 mm to (122.0, 160.2)
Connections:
- X3002 pad 1: /Thread [3]/nRF_XC2 -> /Thread [3]/nRF_XC1
- X3002 pad 2: /Thread [3]/nRF_XC1 -> GND
- X3002 pad 3: (no net) -> /Thread [3]/nRF_XC2
- X3002 pad 4: (no net) -> GND

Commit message: Added net classes and colouring on layout editor
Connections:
- net /USB and SD [7]/SoC_SD_CLK renamed /USB and SD [7]/SD_SoC_CLK
- net Net-(U1001D-DDR0_CAL0) renamed /Memory [5]/DDR_CAL0

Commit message: Fixed footprint issues to comply with manufacturer constraints
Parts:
- moved U5001 113.9 mm to (49.0, 102.3)
- moved U1001 87.7 mm to (51.4, 78.3), turned to 90 degrees
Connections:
- net /Host System [1]/SoC_I2C_SCL renamed /Host System [1]/I2C_SCL_SoC
- R7018 pad 2: /USB and SD [7]/USB0_RCALIB -> /USB and SD [7]/USB1_RCALIB
- U1001 pad AC9: /USB and SD [7]/USB0_RCALIB -> /USB and SD [7]/USB1_RCALIB

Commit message: More layout
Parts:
- moved C1002 153.0 mm to (419.9, 69.9)
- moved C1003 153.0 mm to (419.9, 71.8)
- moved C1004 153.0 mm to (419.9, 73.8)
- moved C1006 153.0 mm to (419.9, 75.8)
- moved C1008 153.0 mm to (282.7, 165.3)
- moved C1009 153.0 mm to (282.7, 167.3)
- moved C3001 153.0 mm to (274.4, 169.0)
- moved C3002 153.0 mm to (278.1, 165.2)
- moved C3003 153.0 mm to (278.1, 167.0)
- moved C4021 153.0 mm to (368.3, 50.2)
- moved C4022 153.0 mm to (368.3, 52.0)
- moved C4023 153.0 mm to (368.3, 53.7)
- moved C4024 153.0 mm to (368.3, 55.5)
- moved C4025 153.0 mm to (368.3, 57.2)
- moved C4026 153.0 mm to (368.3, 59.0)
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
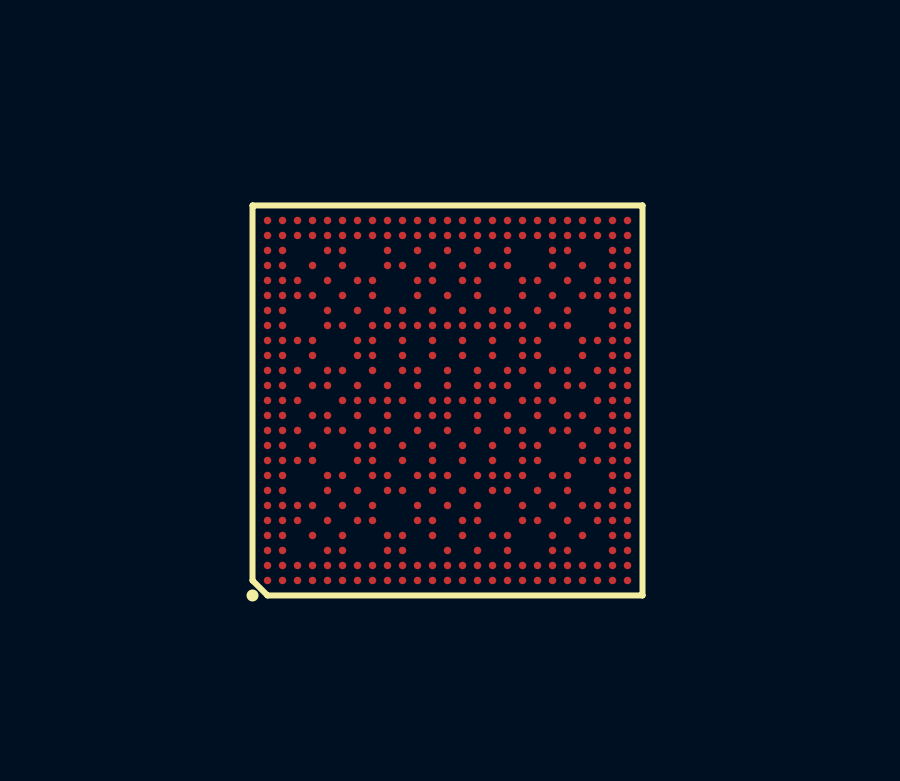
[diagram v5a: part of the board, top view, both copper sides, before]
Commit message: Did fanout for SoC BGA power balls
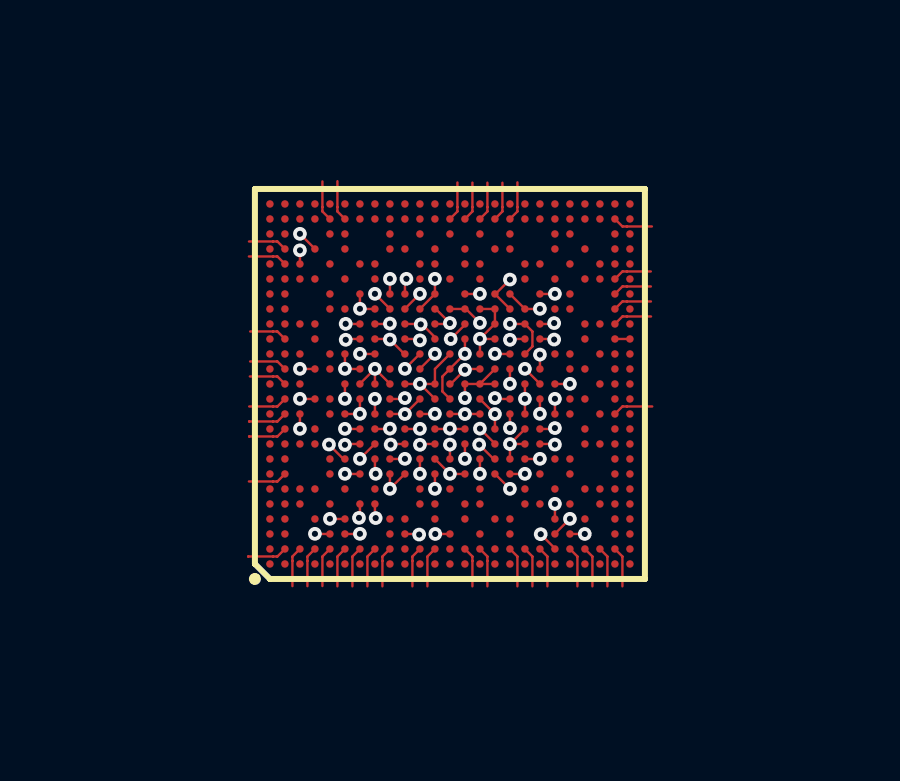
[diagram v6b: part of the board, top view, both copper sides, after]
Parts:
- moved U1001 0.56 mm to (148.8, 131.1)
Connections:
- net /Power Circuitry [4]/SoC_VPP renamed /Power Circuitry [4]/VDD_SoC_VPP
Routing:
- net GND: track 0.00 -> 24.4 mm, vias 0 -> 19
- net VDD_CORE: track 0.00 -> 9.77 mm, vias 0 -> 11
- net VDD_1V8: track 0.00 -> 6.50 mm, vias 0 -> 8
- net VDDA_0V85: track 0.00 -> 5.17 mm, vias 0 -> 5
- net VDD_3V3: track 0.00 -> 3.92 mm, vias 0 -> 5
- net VDD_1V2: track 0.00 -> 2.48 mm, vias 0 -> 5
- net VDDA_1V8: track 0.00 -> 1.70 mm, vias 0 -> 3
- net /Host System [1]/EEP_WP: track 0.00 -> 1.36 mm
- net UART5_TXD: track 0.00 -> 1.35 mm
- net /USB and SD [7]/USB0_DP: track 0.00 -> 1.35 mm
- net /USB and SD [7]/EMMC_D7: track 0.00 -> 1.35 mm
- net /USB and SD [7]/EMMC_D6: track 0.00 -> 1.35 mm
- net /USB and SD [7]/EMMC_D4: track 0.00 -> 1.35 mm
- net /USB and SD [7]/EMMC_D0: track 0.00 -> 1.35 mm
- net /Memory [5]/DDR_UDQS_N: track 0.00 -> 1.35 mm
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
